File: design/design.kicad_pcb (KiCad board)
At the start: 2 copper layers, 176.5 x 83.2 mm, 24 parts, among them J2 Conn_01x08_Socket, SW1 SW_Push, SW10 SW_Push, SW11 SW_Push, SW12 SW_Push, SW13 SW_Push, SW2 SW_Push, SW3 SW_Push, SW4 SW_Push, SW5 SW_Push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

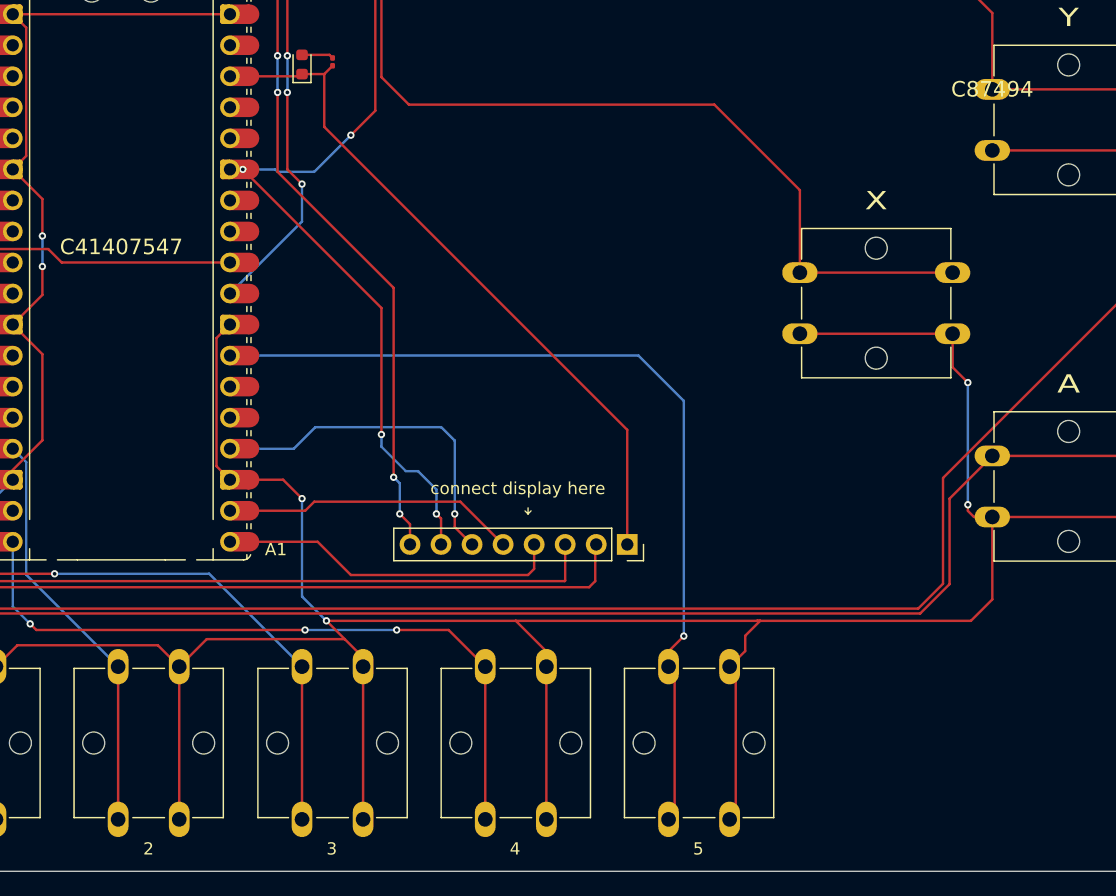
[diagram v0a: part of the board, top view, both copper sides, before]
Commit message: Reorganised file structure, interactive BOM
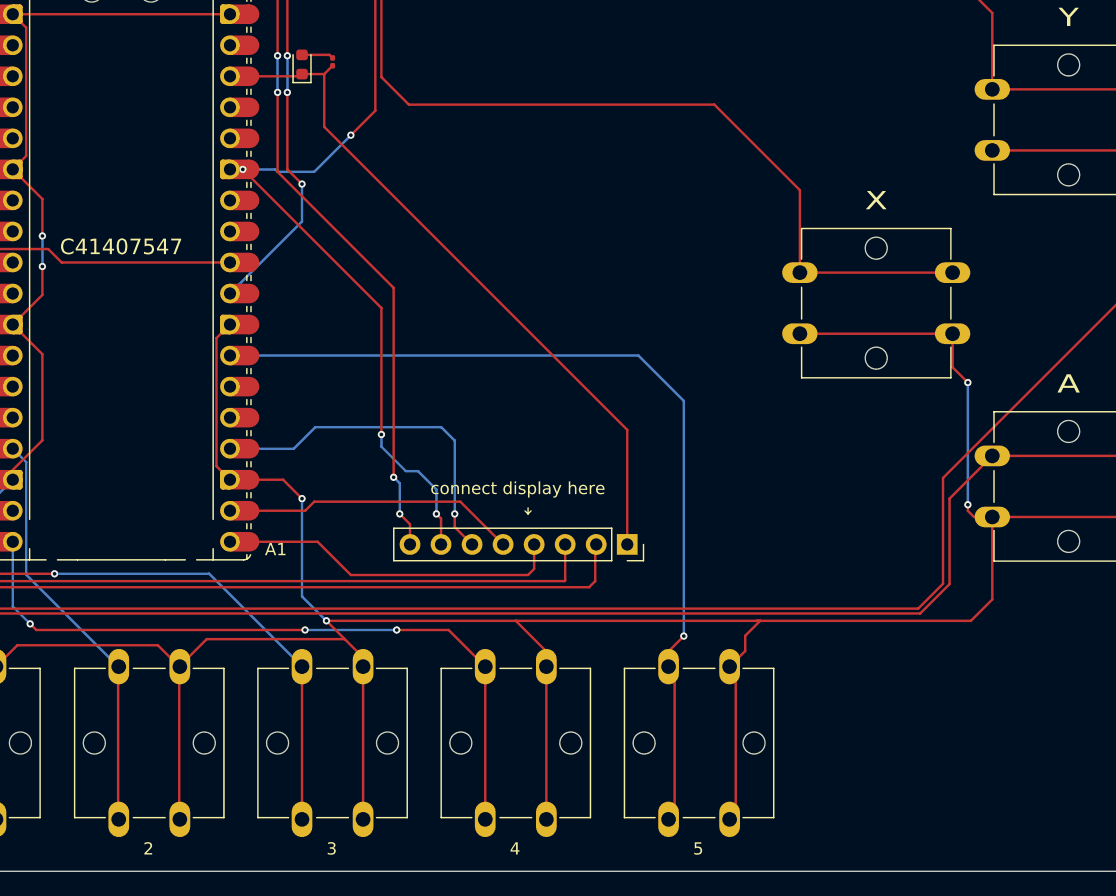
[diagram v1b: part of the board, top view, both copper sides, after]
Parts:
- moved SW10 0.05 mm to (137.5, 137.5)
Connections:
- SW1 pad 1: Net-(A1-GPIO0) -> (no net)
- SW1 pad 2: Net-(S2-A) -> (no net)
- SW10 pad 1: Net-(A1-GPIO13) -> (no net)
- SW10 pad 2: Net-(S2-A) -> (no net)

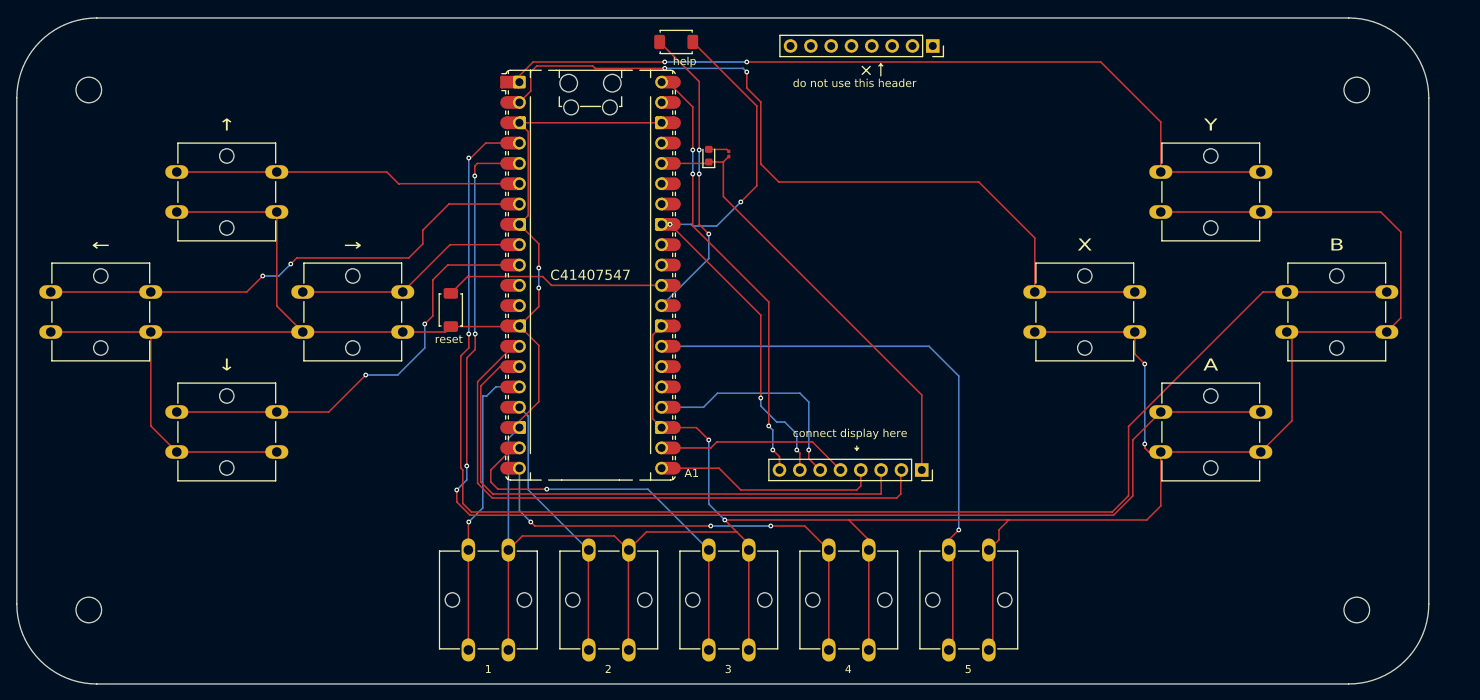
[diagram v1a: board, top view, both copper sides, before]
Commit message: Adding gyroscope, redesigning PCB
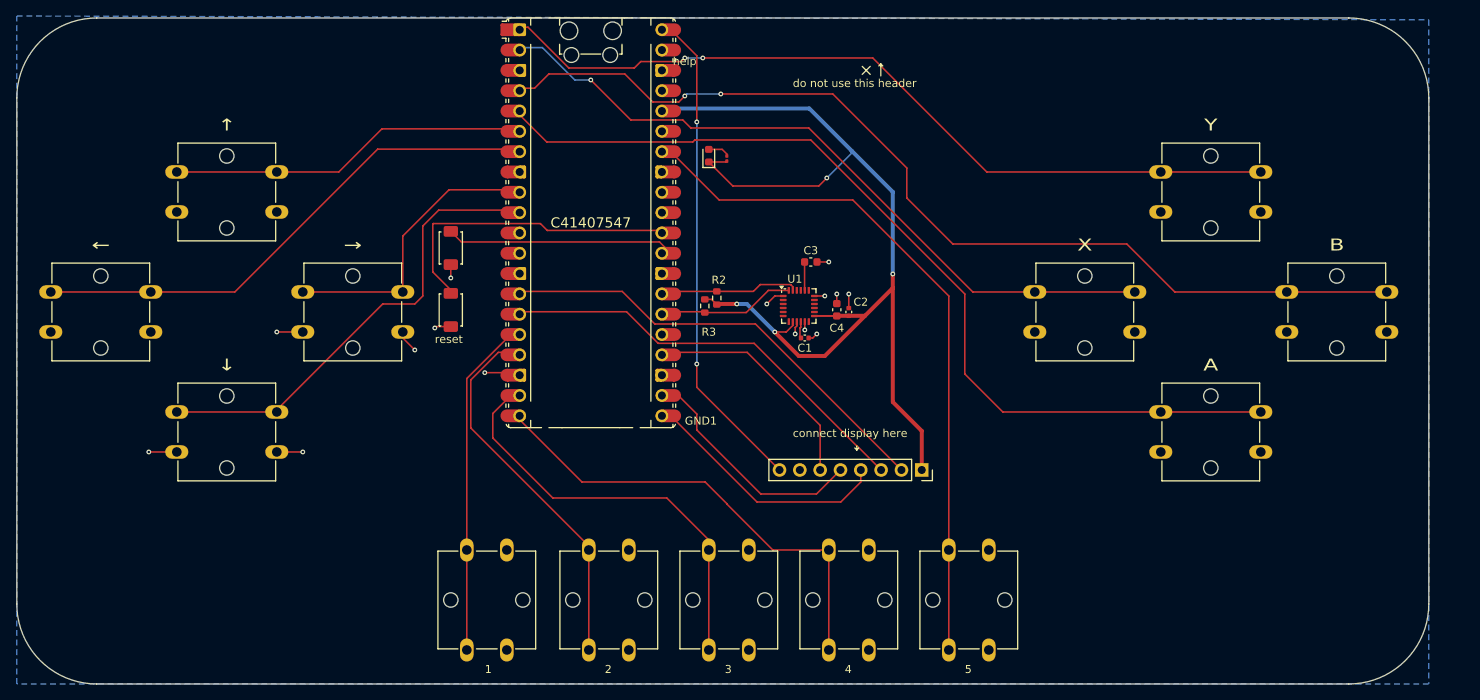
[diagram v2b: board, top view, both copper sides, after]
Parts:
- removed the J2 at (180.5, 62.0)
- removed REF** (x4): MountingHole_3.2mm_M3, MountingHole:MountingHole_3.2mm_M3
- added C1: 0.1uF, Capacitor_SMD:C_0402_1005Metric, F.Cu at (164.5, 98.5)
- added C2: 0.1uF, Capacitor_SMD:C_0402_1005Metric, F.Cu at (170.0, 95.2)
- added C3: 2.2nF, Capacitor_SMD:C_0603_1608Metric, F.Cu at (165.2, 89.0)
- added C4: 10nF, Capacitor_SMD:C_0603_1608Metric, F.Cu at (168.5, 95.0)
- added R2: 4.7k, Resistor_SMD:R_0603_1608Metric, F.Cu at (153.5, 93.5)
- added R3: 4.7k, Resistor_SMD:R_0603_1608Metric, F.Cu at (152.0, 94.5)
- added U1: MPU-6050, Sensor_Motion:InvenSense_QFN-24_4x4mm_P0.5mm, F.Cu at (163.8, 94.5)
- moved S1 38.2 mm to (120.2, 87.2), turned to -90 degrees
- moved GND1 6.55 mm to (137.8, 84.1)
- moved R1 0.62 mm to (154.8, 76.1)
- moved SW9 0.20 mm to (122.2, 137.5)
- renumbered A1 to GND1
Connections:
- net /LED renamed /3V3
- GND1 pad 1: Net-(A1-GPIO0) -> Net-(GND1-GPIO0)
- GND1 pad 13: Net-(S2-A) -> GND
- GND1 pad 17: Net-(A1-GPIO13) -> Net-(GND1-GPIO13)
- GND1 pad 18: Net-(S2-A) -> GND
- GND1 pad 23: Net-(S2-A) -> GND
- GND1 pad 26: unconnected-(A1-GPIO20-Pad26)_1 -> Net-(GND1-GPIO20)
- GND1 pad 27: Net-(A1-GPIO21) -> Net-(GND1-GPIO21)
- GND1 pad 28: Net-(S2-A) -> GND
- GND1 pad 3: Net-(S2-A) -> GND
- GND1 pad 33: /GND -> GND
- GND1 pad 34: unconnected-(A1-GPIO28_ADC2-Pad34) -> Net-(GND1-GPIO28_ADC2)
- GND1 pad 38: Net-(S2-A) -> GND
- GND1 pad 8: Net-(S2-A) -> GND
- J2 pad 7: /GND -> GND
- S1 pad 2: /GND -> GND
- S2 pad 1: Net-(S2-A) -> GND
- SW1 pad 1: (no net) -> Net-(GND1-GPIO0)
- SW1 pad 2: (no net) -> GND
- SW10 pad 1: (no net) -> Net-(GND1-GPIO13)
- SW10 pad 2: (no net) -> GND
- SW11 pad 2: Net-(S2-A) -> GND
- SW12 pad 2: Net-(S2-A) -> GND
- SW13 pad 1: Net-(A1-GPIO21) -> Net-(GND1-GPIO28_ADC2)
- SW13 pad 2: Net-(S2-A) -> GND
- SW2 pad 2: Net-(S2-A) -> GND
- SW3 pad 2: Net-(S2-A) -> GND
- SW4 pad 2: Net-(S2-A) -> GND
- SW5 pad 2: Net-(S2-A) -> GND
- SW6 pad 2: Net-(S2-A) -> GND
- SW7 pad 2: Net-(S2-A) -> GND
- SW8 pad 2: Net-(S2-A) -> GND
- SW9 pad 2: Net-(S2-A) -> GND
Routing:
- net Net-(S2-A): track 510.3 -> 0.00 mm, vias 6 -> 0
- net Net-(A1-GPIO0): track 103.9 -> 0.00 mm, vias 2 -> 0
- net Net-(GND1-GPIO0): track 0.00 -> 101.2 mm, vias 0 -> 2
- net Net-(GND1-GPIO28_ADC2): track 0.00 -> 86.9 mm
- net /3V3: track 56.7 -> 132.2 mm, vias 0 -> 4
- net Net-(A1-GPIO21): track 73.5 -> 0.00 mm, vias 1 -> 0
- net /GND: track 73.4 -> 0.00 mm, vias 4 -> 0
- net Net-(GND1-GPIO2): track 182.4 -> 123.4 mm
- net Net-(GND1-GPIO13): track 0.00 -> 46.6 mm
- net Net-(GND1-GPIO3): track 158.5 -> 115.2 mm, vias 4 -> 0
- net Net-(A1-GPIO13): track 33.9 -> 0.00 mm
- net GND: track 0.00 -> 32.6 mm, vias 0 -> 15
- net /SCK: track 75.9 -> 57.8 mm
- net /SDA: track 70.7 -> 53.4 mm
- net Net-(GND1-GPIO21): track 0.00 -> 16.5 mm
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- added copper zone on B.Cu, net GND

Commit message: Added details on parts, added gyroscope to design
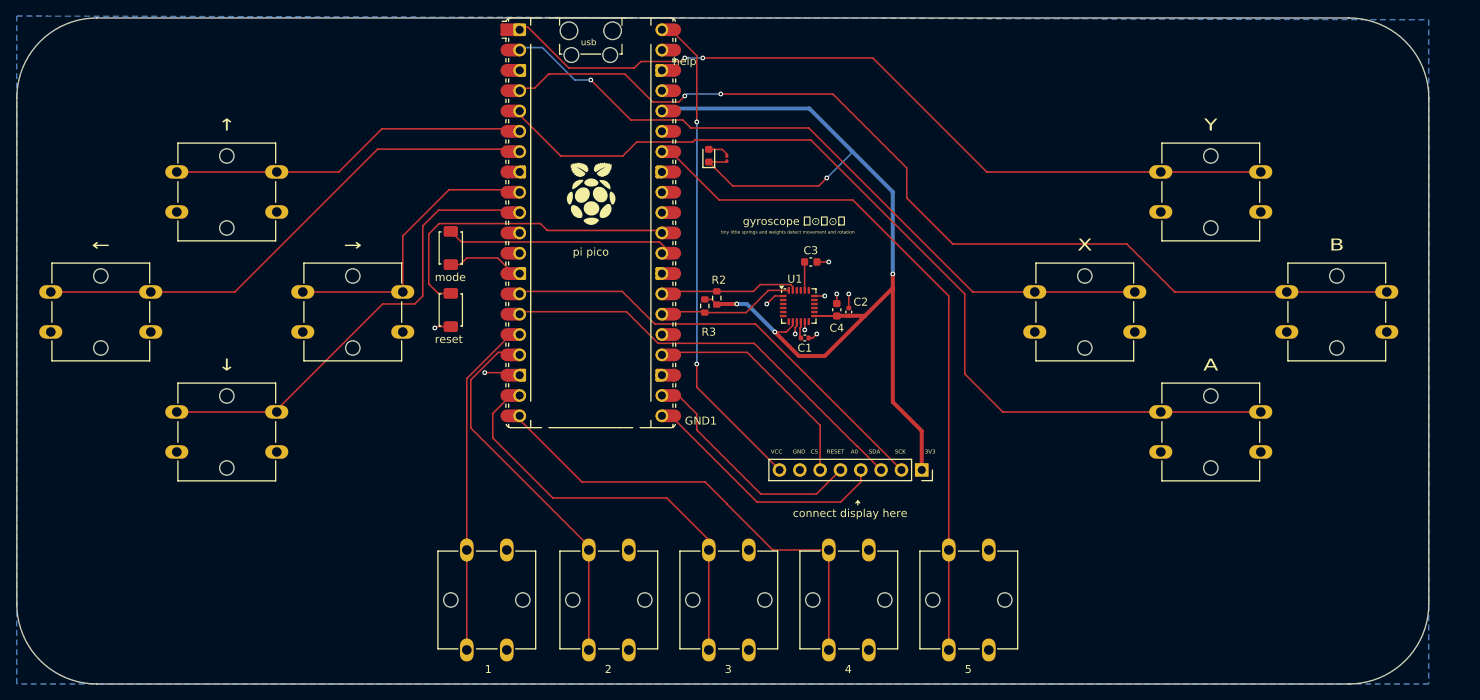
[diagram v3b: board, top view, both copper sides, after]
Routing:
- net GND: track 32.6 -> 27.7 mm, vias 15 -> 10
- net Net-(GND1-GPIO3): track 115.2 -> 116.7 mm
- net Net-(GND1-RUN): track 39.4 -> 40.3 mm
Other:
- board text added: "3V3"
- board text added: "A0"
- board text added: "CS"
- board text added: "GND"
- board text added: "RESET"
- board text added: "SCK"
- board text added: "SDA"
- board text added: "VCC"
- board text added: "gyroscope （⊙ｏ⊙）"
- board text added: "mode"
- board text added: "tiny little springs and weights detect movement and rotation"
- board text added: "usb"
- board text removed: "do not use this header"

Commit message: Design updates and add MPU6050 driver
Update KiCad PCB, gerbers and BOM; adjust STEP/3D model coordinates and add new 3D/production STL assets. Tidy repo by updating .gitignore and adding a VSCode setting. Remove outdated production bundles (ManufacturedPart.stl, gerber.zip, part-positions.csv) and add case STLs, position file and KiCad lock files. Update README with an MPU6050 link, modify software/main.py and add software/mpu6050.py to support the MPU6050 sensor.
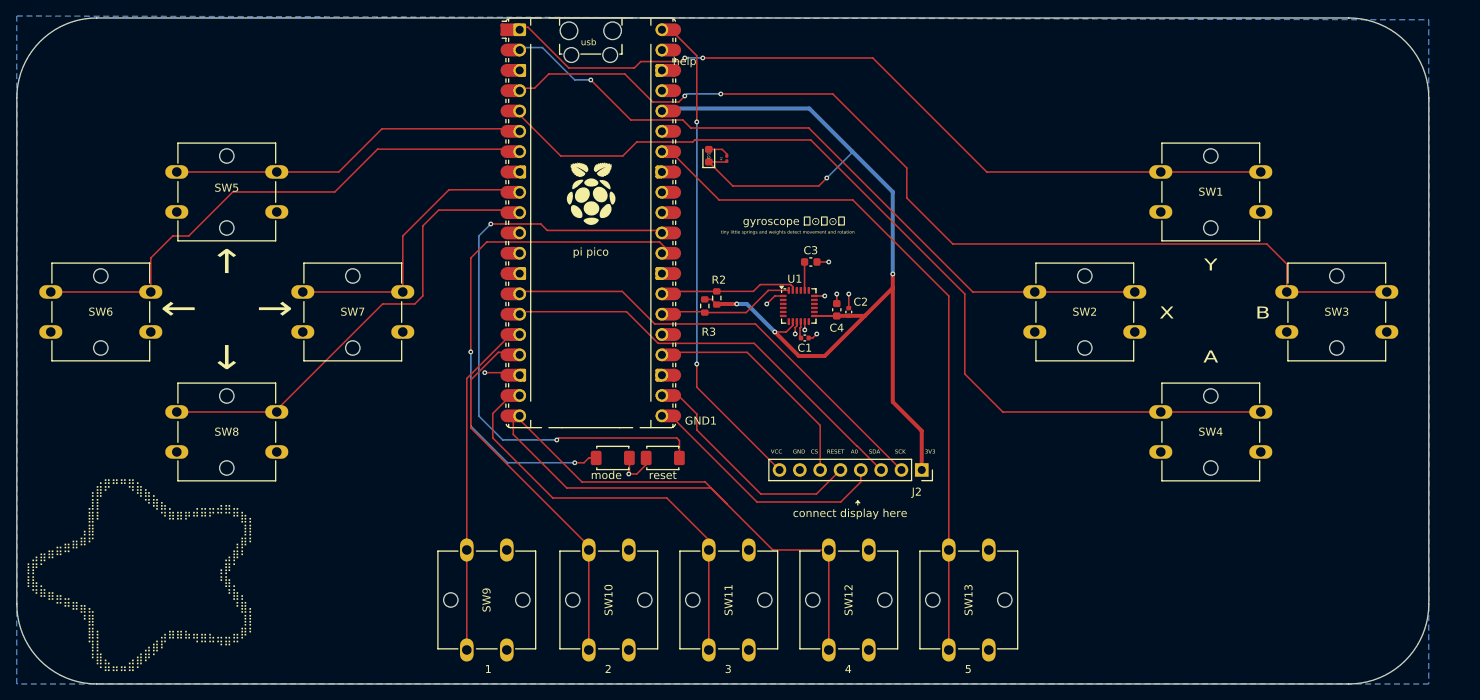
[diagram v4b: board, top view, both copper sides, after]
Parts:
- moved S1 33.2 mm to (140.5, 113.5), turned to 0 degrees
- moved S2 32.3 mm to (146.8, 113.5), turned to 0 degrees
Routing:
- net Net-(GND1-GPIO22): track 28.2 -> 64.8 mm, vias 0 -> 2
- net Net-(GND1-RUN): track 40.3 -> 75.9 mm, vias 0 -> 2
- net Net-(GND1-GPIO15): track 59.0 -> 91.7 mm
- net GND: track 27.7 -> 22.2 mm
- net Net-(GND1-GPIO5): track 66.0 -> 68.5 mm
- net Net-(GND1-GPIO2): track 123.4 -> 125.5 mm
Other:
- board text added: "⠀⠀⠀⠀⠀⠀⠀⠀⠀⢀⣤⣤⣤⣤⡀⠀⠀⠀⠀⠀⠀⠀⠀⠀⠀⠀⠀⠀⠀ ⠀⠀⠀⠀⠀⠀⠀⠀⢠⣿⠋⠀⠀⠙⢿⣦⡀⠀⠀⠀⠀⠀⠀⠀⠀⠀⠀⠀⠀ ⠀⠀⠀⠀⠀⠀⠀⠀⣸⡇⠀⠀⠀⠀⠀⠙⢿⣦⡀⠀⠀⢀⣀⣀⣠⣤⣀⠀⠀ ⠀⠀⠀⠀⠀⠀⠀⠀⣿⠇⠀⠀⠀⠀⠀⠀⠀⠙⠿⠿⠟⠛⠛⠋⠉⠉⠛⣷⡄ ⠀⠀⠀⠀⠀⠀⠀⢠⣿⠀⠀⠀⠀⠀⠀⠀⠀⠀⠀⠀⠀⠀⠀⠀⠀⠀⠀⢸⡇ ⠀⠀⠀⠀⣀⣤⣶⠿⠋⠀⠀⠀⠀⠀⠀⠀⠀⠀⠀⠀⠀⠀⠀⠀⠀⠀⢠⡿⠃ ⠀⣠⣶⠿⠛⠉⠀⠀⠀⠀⠀⠀⠀⠀⠀⠀⠀⠀⠀⠀⠀⠀⠀⠀⠀⣠⡿⠃⠀ ⢸⡟⠁⠀⠀⠀⠀⠀⠀⠀⠀⠀⠀⠀⠀⠀⠀⠀⠀⠀⠀⠀⠀⠀⢠⡿⠁⠀⠀ ⢸⣧⡀⠀⠀⠀⠀⠀⠀⠀⠀⠀⠀⠀⠀⠀⠀⠀⠀⠀⠀⠀⠀⠀⠘⣷⡀⠀⠀ ⠀⠙⠿⣶⣤⣀⠀⠀⠀⠀⠀⠀⠀⠀⠀⠀⠀⠀⠀⠀⠀⠀⠀⠀⠀⠘⣷⡄⠀ ⠀⠀⠀⠀⠉⠛⠿⣶⣄⠀⠀⠀⠀⠀⠀⠀⠀⠀⠀⠀⠀⠀⠀⠀⠀⠀⠘⣿⡄ ⠀⠀⠀⠀⠀⠀⠀⠘⣿⠀⠀⠀⠀⠀⠀⠀⠀⠀⠀⠀⠀⠀⠀⠀⠀⠀⠀⢸⡇ ⠀⠀⠀⠀⠀⠀⠀⠀⣿⡆⠀⠀⠀⠀⠀⠀⠀⣠⣶⣶⣦⣤⣤⣄⣀⣀⣤⡿⠃ ⠀⠀⠀⠀⠀⠀⠀⠀⢹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"

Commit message: Improved poster and renders, re-exported gerber file
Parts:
- added REF**: MountingHole_3.2mm_M3, MountingHole:MountingHole_3.2mm_M3, F.Cu at (233.5, 67.5)
- added REF**: MountingHole_3.2mm_M3, MountingHole:MountingHole_3.2mm_M3, F.Cu at (233.5, 132.5)
- added REF**: MountingHole_3.2mm_M3, MountingHole:MountingHole_3.2mm_M3, F.Cu at (75.0, 132.5)
- added REF**: MountingHole_3.2mm_M3, MountingHole:MountingHole_3.2mm_M3, F.Cu at (75.0, 67.5)
